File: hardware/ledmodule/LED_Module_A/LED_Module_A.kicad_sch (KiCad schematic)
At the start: 140 parts, among them J2 To MAIN_MOD, U1 DS18B20U

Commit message: Preparation for fabrication
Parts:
- added H1, H2, H3, H4, H5, H6, H7: MountingHole, MountingHole:MountingHole_3.2mm_M3, symbol Mechanical:MountingHole
- D_R1, D_R2, D_R3, D_R4, D_R5, D_R6, D_R7, D_R8: value Photo Red -> Red; Mouser Part 941-JE2835AHRN01AN -> 941-JE2835ARDN01AN
- J2: now not fitted; now left out of the parts list

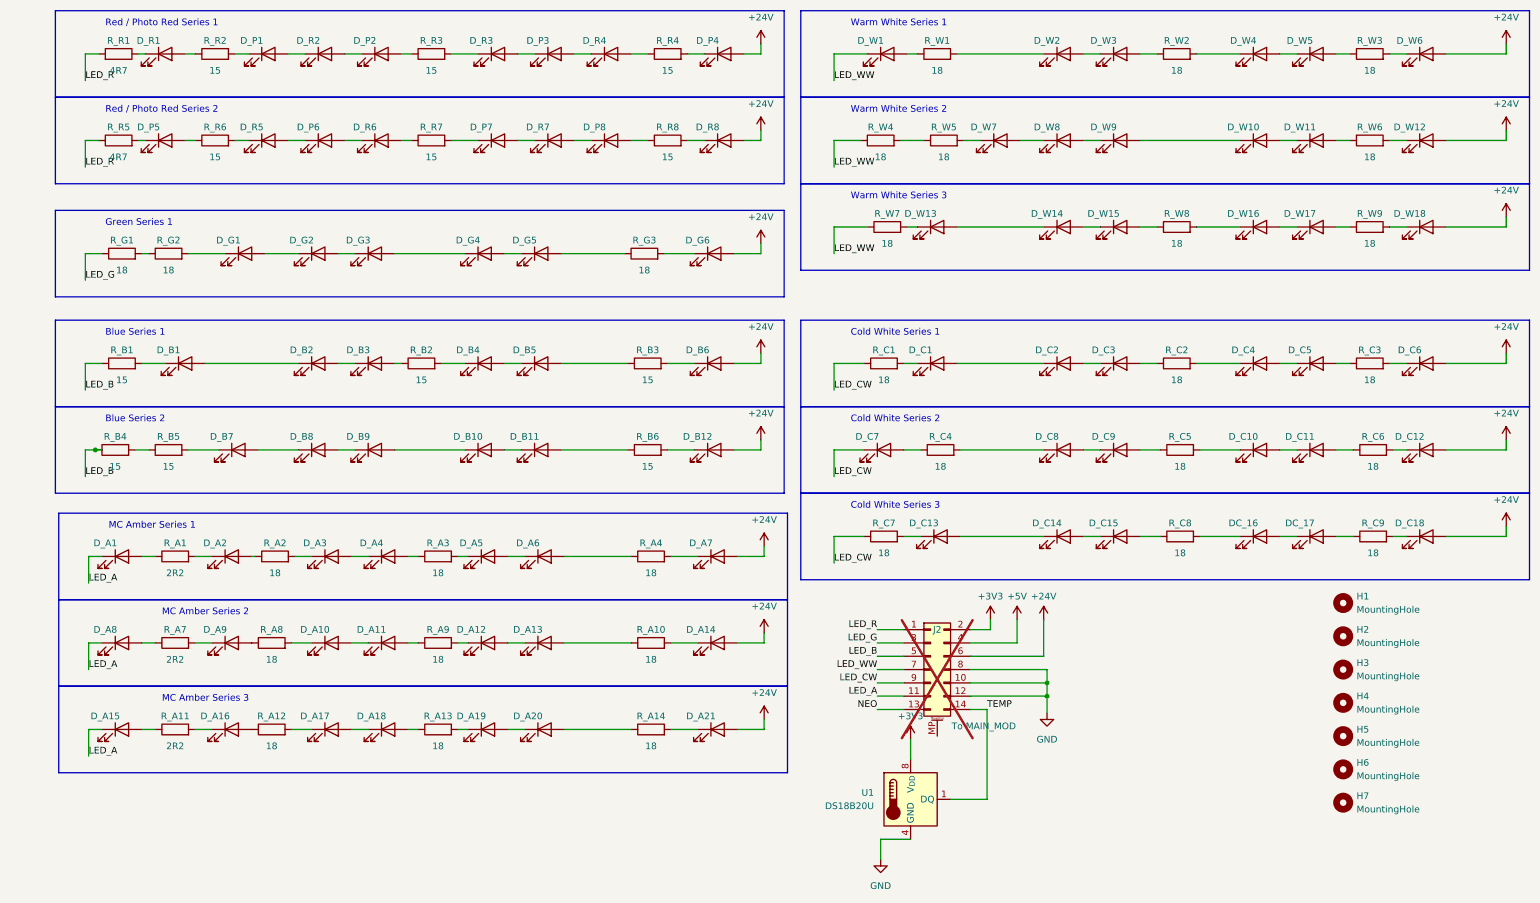
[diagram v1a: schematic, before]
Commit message: Ready for production - but needs expensive hole plating.
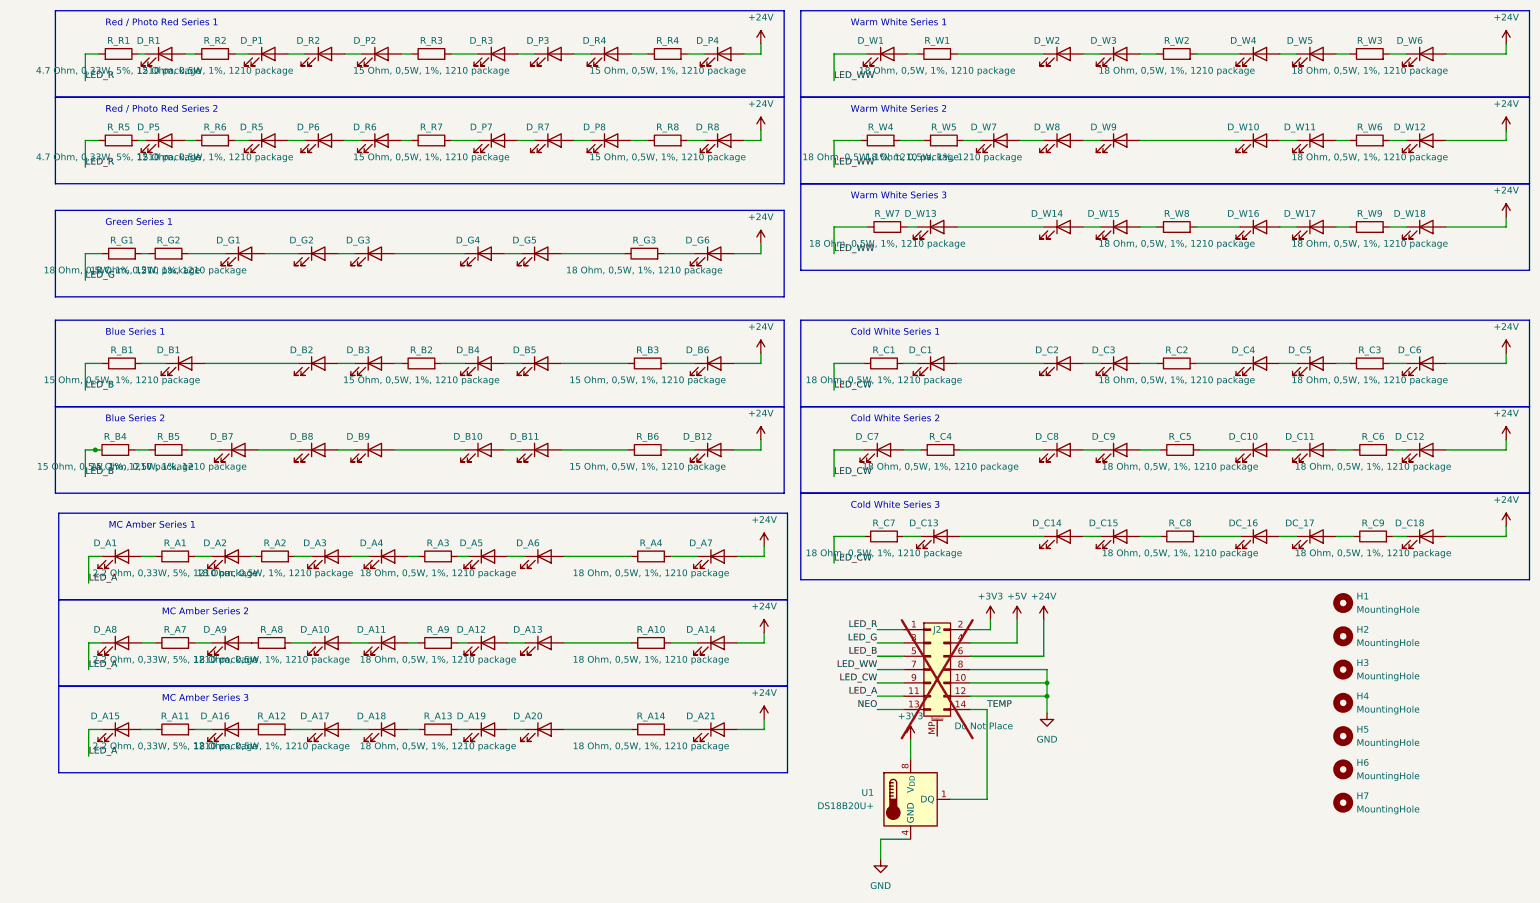
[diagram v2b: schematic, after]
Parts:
- DC_16, DC_17, D_C1, D_C10, D_C11, D_C12, D_C13, D_C14, D_C15, D_C18, D_C2, D_C3, D_C4, D_C5, D_C6, D_C7, D_C8, D_C9: Manufacturer (none) -> Cree LED; Part Number (none) -> JE2835BWT-N-U57GA0000-N0000001
- D_A1, D_A10, D_A11, D_A12, D_A13, D_A14, D_A15, D_A16, D_A17, D_A18, D_A19, D_A2, D_A20, D_A21, D_A3, D_A4, D_A5, D_A6, D_A7, D_A8, D_A9: Manufacturer (none) -> Cree LED; Part Number (none) -> JE2835AAM-N-0001A0000-N0000001
- D_B1, D_B10, D_B11, D_B12, D_B2, D_B3, D_B4, D_B5, D_B6, D_B7, D_B8, D_B9: Manufacturer (none) -> Cree LED; Part Number (none) -> JE2835ABL-N-0005A0000-N0000001
- D_G1, D_G2, D_G3, D_G4, D_G5, D_G6: Manufacturer (none) -> Cree LED; Part Number (none) -> JE2835AGR-N-0002A0000-N0000001
- D_P1, D_P2, D_P3, D_P4, D_P5, D_P6, D_P7, D_P8: Manufacturer (none) -> Cree LED; Part Number (none) -> JE2835AHR-N-0001A0000-N0000001
- D_R1, D_R2, D_R3, D_R4, D_R5, D_R6, D_R7, D_R8: Manufacturer (none) -> Cree LED; Part Number (none) -> JE2835ARD-N-0001A0000-N0000001
- D_W1, D_W10, D_W11, D_W12, D_W13, D_W14, D_W15, D_W16, D_W17, D_W18, D_W2, D_W3, D_W4, D_W5, D_W6, D_W7, D_W8, D_W9: Manufacturer (none) -> Cree LED; Part Number (none) -> JE2835BWT-N-U30GA0000-N0000001
- H1, H2, H3, H4, H5, H6, H7: Note (none) -> Just drill, no part to place; Specification (none) -> MountingHole
- J2: value To MAIN_MOD -> Do Not Place; Note (none) -> Do Not Place
- R_A1, R_A11, R_A7: value 2R2 -> 2.2 Ohm, 0,33W, 5%, 1210 package; Specification (none) -> 2.2 Ohm, 0,33W, 5%, 1210 package
- R_A10, R_A12, R_A13, R_A14, R_A2, R_A3, R_A4, R_A8, R_A9, R_C1, R_C2, R_C3, R_C4, R_C5, R_C6, R_C7, R_C8, R_C9, R_G1, R_G2, R_G3, R_W1, R_W2, R_W3, R_W4, R_W5, R_W6, R_W7, R_W8, R_W9: value 18 -> 18 Ohm, 0,5W, 1%, 1210 package; Specification (none) -> 18 Ohm, 0,5W, 1%, 1210 package
- R_B1, R_B2, R_B3, R_B4, R_B5, R_B6, R_R2, R_R3, R_R4, R_R6, R_R7, R_R8: value 15 -> 15 Ohm, 0,5W, 1%, 1210 package; Specification (none) -> 15 Ohm, 0,5W, 1%, 1210 package
- R_R1, R_R5: value 4R7 -> 4.7 Ohm, 0,33W, 5%, 1210 package; Specification (none) -> 4.7 Ohm, 0,33W, 5%, 1210 package
- U1: value DS18B20U -> DS18B20U+; Manufacturer (none) -> Analog Devices / Maxim Integrated; Note (none) -> Only original parts; Part Number (none) -> DS18B20U+

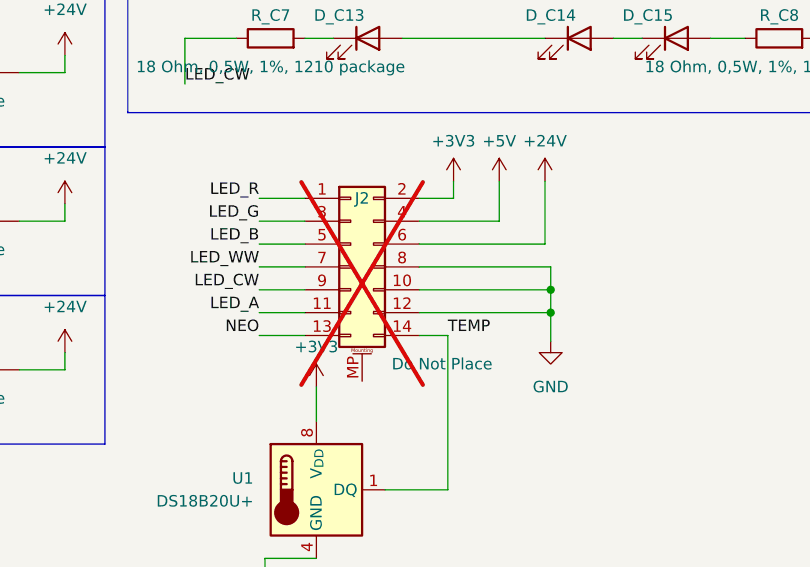
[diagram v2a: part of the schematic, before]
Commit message: SMD pin headers with 90deg rotation
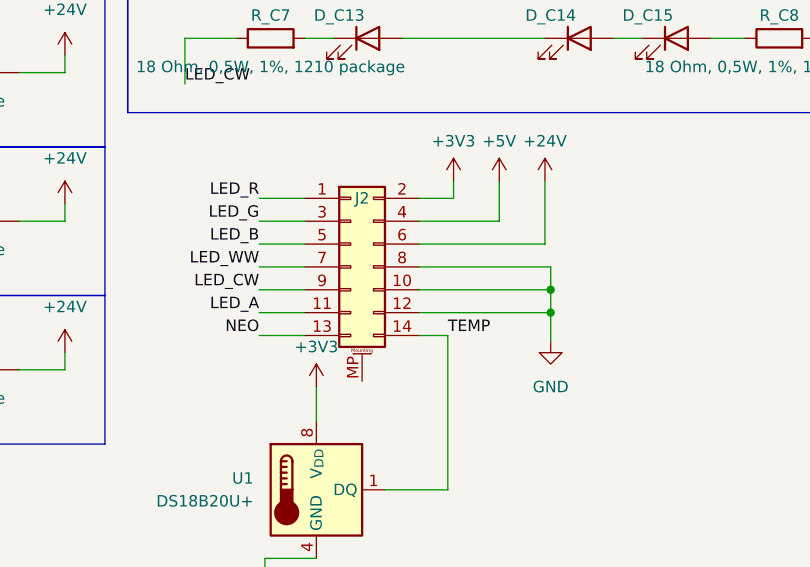
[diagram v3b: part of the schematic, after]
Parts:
- J2: value Do Not Place -> ~; footprint Connector_PinHeader_2.54mm:PinHeader_2x07_P2.54mm_Vertical_Boxed -> Connector_PinHeader_2.54mm:PinHeader_2x07_P2.54mm_Vertical_SMD; Note Do Not Place -> (none); now fitted; now in the parts list
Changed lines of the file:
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@@
   )
   (symbol (lib_id "Connector_Generic_MountingPin:Conn_02x07_Odd_Even_MountingPin") (at 182.245 142.24 0) (unit 1)
-    (in_bom no) (on_board yes) (dnp yes)
+    (in_bom yes) (on_board yes) (dnp no)
     (property "Reference" "J2" (at 183.515 134.62 0)
       (effects (font (size 1.27 1.27)))
     )
-    (property "Value" "Do Not Place" (at 192.405 153.035 0)
+    (property "Value" "~" (at 192.405 153.035 0)
       (effects (font (size 1.27 1.27)))
     )
-    (property "Footprint" "Connector_PinHeader_2.54mm:PinHeader_2x07_P2.54mm_Vertical_Boxed" (at 182.245 142.24 0)
+    (property "Footprint" "Connector_PinHeader_2.54mm:PinHeader_2x07_P2.54mm_Vertical_SMD" (at 182.245 142.24 0)
       (effects (font (size 1.27 1.27)) hide)
     )
@@
       (effects (font (size 1.27 1.27)) hide)
     )
-    (property "Note" "Do Not Place" (at 182.245 142.24 0)
+    (property "Note" "" (at 182.245 142.24 0)
       (effects (font (size 1.27 1.27)) hide)
     )

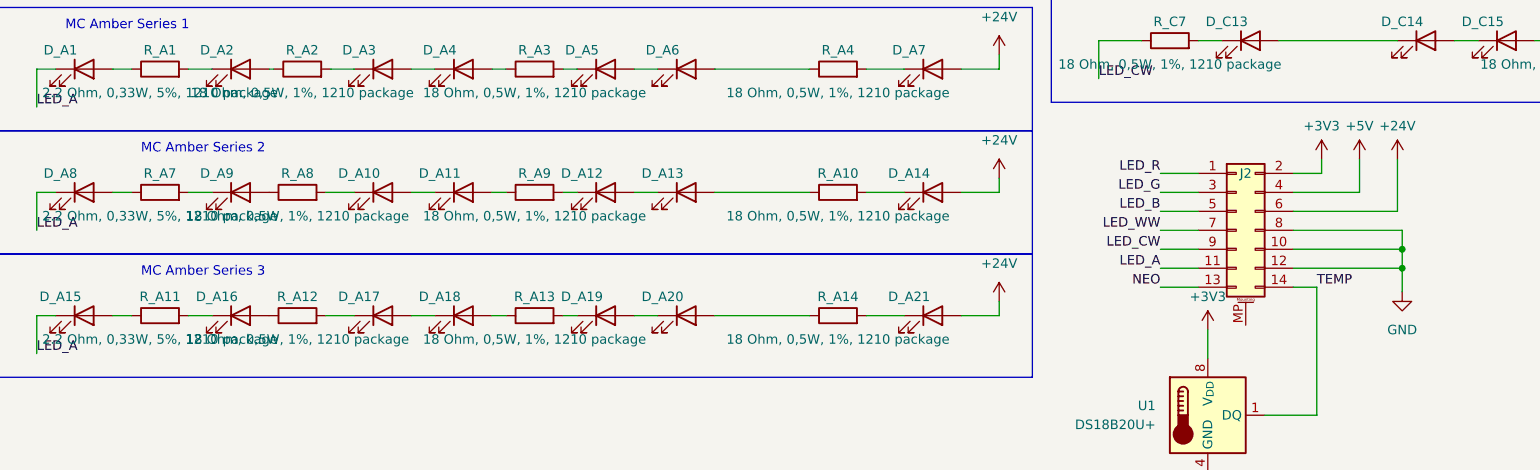
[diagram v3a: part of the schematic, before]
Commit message: New layout with angled SMD header, but probably not aligned correctly.
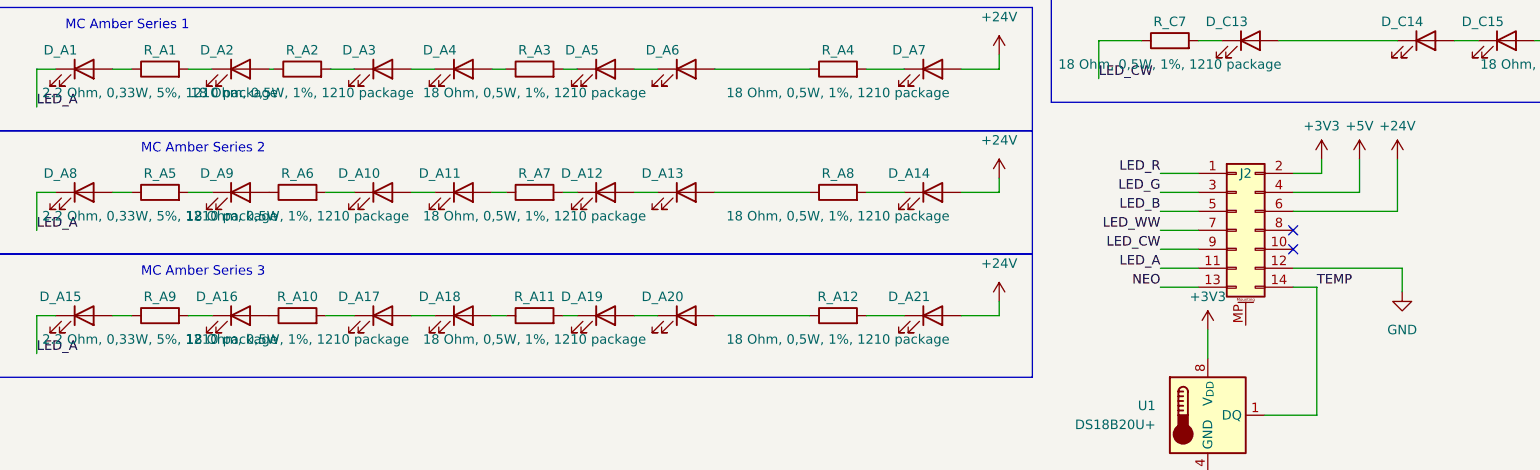
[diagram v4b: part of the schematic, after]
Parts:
- D_A1, D_A10, D_A11, D_A12, D_A13, D_A14, D_A15, D_A16, D_A17, D_A18, D_A19, D_A2, D_A20, D_A21, D_A3, D_A4, D_A5, D_A6, D_A7, D_A8, D_A9, D_P1, D_P2, D_P3, D_P4, D_P5, D_P6, D_P7, D_P8, D_R1, D_R2, D_R3, D_R4, D_R5, D_R6, D_R7, D_R8: footprint LED_SMD:LED_2835_CREE_JSE28L3E5 -> LED_SMD:LED_2835_CREE_JSE28L3E5_Big_Anode
- renumbered R_A12 to R_A10, R_A13 to R_A11, R_A14 to R_A12, R_A7 to R_A5, R_A8 to R_A6, R_A9 to R_A7, R_A10 to R_A8, R_A11 to R_A9
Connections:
- net GND: no longer J2.10 (Pin_10), J2.8 (Pin_8)
- no-connect marks 0 -> 2

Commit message: And yet another connector. This one should be perfect!
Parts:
- J2: footprint Connector_PinHeader_2.54mm:PinHeader_2x07_P2.54mm_Vertical_SMD -> Pin Header Wuerth:610114249121; symbol Connector_Generic_MountingPin:Conn_02x07_Odd_Even_MountingPin -> PinHeaderWuerth:610114249121; Availability (none) -> In Stock; Check_prices (none) -> https://www.snapeda.com/parts/610114249121/Wurth+Elektronik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; MF (none) -> Wurth Elektronik; MP (none) -> 610114249121; Package (none) -> None; Price (none) -> None; Purchase-URL (none) -> https://www.snapeda.com/api/url_track_click_mouser/?unipart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; SnapEDA_Link (none) -> https://www.snapeda.com/parts/610114249121/Wurth+Elektronik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
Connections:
- net +24V: now also J2.5; no longer J2.6 (Pin_6)
- net +3V3: now also J2.1; no longer J2.2 (Pin_2)
- net +5V: now also J2.3; no longer J2.4 (Pin_4)
- net GND: now also J2.11; no longer J2.12 (Pin_12)
- net LED_A: now also J2.12; no longer J2.11 (Pin_11)
- net LED_B: now also J2.6; no longer J2.5 (Pin_5)
- net LED_CW: now also J2.10; no longer J2.9 (Pin_9)
- net LED_G: now also J2.4; no longer J2.3 (Pin_3)
- net LED_R: now also J2.2; no longer J2.1 (Pin_1)
- net LED_WW: now also J2.8; no longer J2.7 (Pin_7)
- net NEO: now also J2.14; no longer J2.13 (Pin_13)
- net TEMP: now also J2.13; no longer J2.14 (Pin_14)
